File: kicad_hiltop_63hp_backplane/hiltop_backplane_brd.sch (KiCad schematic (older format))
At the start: 20 parts

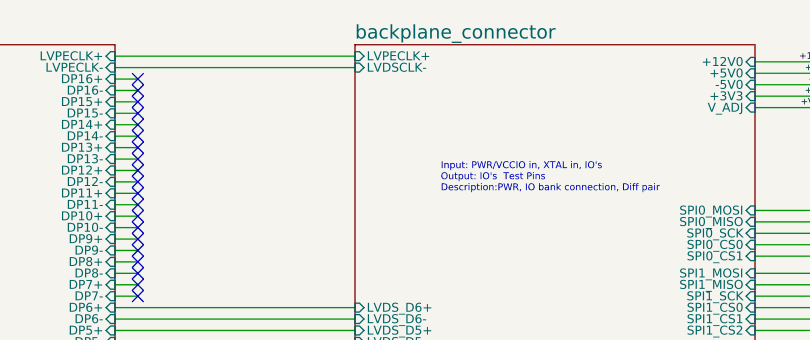
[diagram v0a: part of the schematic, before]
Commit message: pci connector connection moved to bottom layer, FTDI routing and FPGA power routing
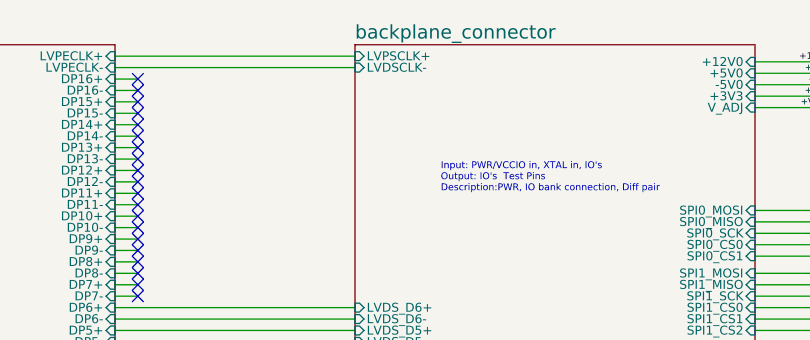
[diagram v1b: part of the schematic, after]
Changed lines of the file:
@@
 F13 "LVDS_D1+" I L 8150 2250 39
 F14 "GND" I R 9900 6250 39
-F15 "LVPECLK+" I L 8150 650 39
+F15 "LVPSCLK+" I L 8150 650 39
 F16 "LVDSCLK-" I L 8150 700 39
 F17 "FPGA_GPIO1" I L 8150 2475 39

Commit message: routing on differential, USB, Power and internconnects
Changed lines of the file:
@@
 F14 "GND" I R 9900 6250 39
 F15 "LVPSCLK+" I L 8150 650 39
-F16 "LVDSCLK-" I L 8150 700 39
+F16 "LVPSCLK-" I L 8150 700 39
 F17 "FPGA_GPIO1" I L 8150 2475 39
 F18 "FPGA_GPIO2" I L 8150 2525 39

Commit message: routing os SODIM and GPIO
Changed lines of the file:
@@
 F35 "MBRD_RESERVED_0" I L 1700 4950 39
 F36 "MBRD_RESERVED_1" I L 1700 5000 39
-F37 "MBRD_RESERVED_2" I R 3700 4950 39
-F38 "MBRD_RESERVED_3" I R 3700 5050 39
+F37 "MBRD_RESERVED_2+" I R 3700 4950 39
+F38 "MBRD_RESERVED_2-" I R 3700 5050 39
 F39 "MBRD_PSEL_0" I L 1700 3525 39
 F40 "MBRD_PSEL_1" I L 1700 3575 39

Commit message: Rev A
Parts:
- R82, R83: symbol device:R -> hiltop_backplane_brd-rescue:R-device
- TP1, TP10, TP11, TP12, TP13, TP16, TP17, TP18, TP19, TP2, TP20, TP3, TP4, TP5, TP6, TP7, TP8, TP9: symbol Connector:TestPoint -> hiltop_backplane_brd-rescue:TestPoint-Connector
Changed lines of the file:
@@
 	7100 4525 8150 4525
 $Comp
-L Connector:TestPoint TP6
+L hiltop_backplane_brd-rescue:TestPoint-Connector TP6
 U 1 1 5C46A039
 P 9975 5050
@@
 $EndComp
 $Comp
-L Connector:TestPoint TP10
+L hiltop_backplane_brd-rescue:TestPoint-Connector TP10
 U 1 1 5C46A4C6
 P 10050 5100
@@
 $EndComp
 $Comp
-L Connector:TestPoint TP7
+L hiltop_backplane_brd-rescue:TestPoint-Connector TP7
 U 1 1 5C46A4E0
 P 9975 5150
@@
 $EndComp
 $Comp
-L Connector:TestPoint TP11
+L hiltop_backplane_brd-rescue:TestPoint-Connector TP11
 U 1 1 5C46A4FC
 P 10050 5200
@@
 $EndComp
 $Comp
-L Connector:TestPoint TP8
+L hiltop_backplane_brd-rescue:TestPoint-Connector TP8
 U 1 1 5C46A522
 P 9975 5250
@@
 $EndComp
 $Comp
-L Connector:TestPoint TP12
+L hiltop_backplane_brd-rescue:TestPoint-Connector TP12
 U 1 1 5C46A542
 P 10050 5300
@@
 $EndComp
 $Comp
-L Connector:TestPoint TP9
+L hiltop_backplane_brd-rescue:TestPoint-Connector TP9
 U 1 1 5C46A566
 P 9975 5350
@@
 $EndComp
 $Comp
-L Connector:TestPoint TP13
+L hiltop_backplane_brd-rescue:TestPoint-Connector TP13
 U 1 1 5C46A590
 P 10050 5400
@@
 	1225 3625 1700 3625
 $Comp
-L Connector:TestPoint TP2
+L hiltop_backplane_brd-rescue:TestPoint-Connector TP2
 U 1 1 5C441846
 P 1275 3675
@@
 $EndComp
 $Comp
-L Connector:TestPoint TP1
+L hiltop_backplane_brd-rescue:TestPoint-Connector TP1
 U 1 1 5C441970
 P 1200 3725
@@
 $EndComp
 $Comp
-L Connector:TestPoint TP3
+L hiltop_backplane_brd-rescue:TestPoint-Connector TP3
 U 1 1 5C4419AA
 P 1275 3775
@@
 	1225 4950 1500 4950
 $Comp
-L Connector:TestPoint TP4
+L hiltop_backplane_brd-rescue:TestPoint-Connector TP4
 U 1 1 5D454C70
 P 1325 4875
@@
 $EndComp
 $Comp
-L Connector:TestPoint TP5
+L hiltop_backplane_brd-rescue:TestPoint-Connector TP5
 U 1 1 5D454D59
 P 1325 5075
@@
 FPGA_RST
 $Comp
-L device:R R82
+L hiltop_backplane_brd-rescue:R-device R82
 U 1 1 5C4B32E3
 P 4200 4950
@@
 $EndComp
 $Comp
-L device:R R83
+L hiltop_backplane_brd-rescue:R-device R83
 U 1 1 5C4B338E
 P 4200 5050
@@
 	4350 4950 4600 4950
 $Comp
-L Connector:TestPoint TP16
+L hiltop_backplane_brd-rescue:TestPoint-Connector TP16
 U 1 1 5C507009
 P 4200 2250
@@
 $EndComp
 $Comp
-L Connector:TestPoint TP19
+L hiltop_backplane_brd-rescue:TestPoint-Connector TP19
 U 1 1 5C507080
 P 4275 2300
@@
 $EndComp
 $Comp
-L Connector:TestPoint TP17
+L hiltop_backplane_brd-rescue:TestPoint-Connector TP17
 U 1 1 5C507107
 P 4200 2350
@@
 $EndComp
 $Comp
-L Connector:TestPoint TP20
+L hiltop_backplane_brd-rescue:TestPoint-Connector TP20
 U 1 1 5C507184
 P 4275 2400
@@
 $EndComp
 $Comp
-L Connector:TestPoint TP18
+L hiltop_backplane_brd-rescue:TestPoint-Connector TP18
 U 1 1 5C507279
 P 4200 2450

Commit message: add latest changes
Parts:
- R82, R83: symbol hiltop_backplane_brd-rescue:R-device -> hiltop_backplane_brd-rescue:R-device-hiltop_backplane_brd-rescue
- TP1, TP10, TP11, TP12, TP13, TP16, TP17, TP18, TP19, TP2, TP20, TP3, TP4, TP5, TP6, TP7, TP8, TP9: symbol hiltop_backplane_brd-rescue:TestPoint-Connector -> hiltop_backplane_brd-rescue:TestPoint-Connector-hiltop_backplane_brd-rescue
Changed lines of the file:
@@
 EESchema Schematic File Version 4
 LIBS:hiltop_backplane_brd-cache
-EELAYER 26 0
+EELAYER 29 0
 EELAYER END
 $Descr A4 11693 8268
 encoding utf-8
 Sheet 1 6
-Title "Project X"
-Date ""
-Rev "Draft"
+Title "63HP HILTOP Backplane"
+Date "2020-02-29"
+Rev "B"
 Comp "Devtank Ltd"
 Comment1 ""
@@
 F99 "USB1_N" I R 9900 4475 39
 F100 "USB1_P" I R 9900 4425 39
-F101 "USB2_N" I R 9900 4525 39
-F102 "USB2_P" I R 9900 4575 39
+F101 "USB2_N" I R 9900 4575 39
+F102 "USB2_P" I R 9900 4525 39
 F103 "USB3_N" I R 9900 4675 39
 F104 "USB3_P" I R 9900 4625 39
@@
 	7100 4525 8150 4525
 $Comp
-L hiltop_backplane_brd-rescue:TestPoint-Connector TP6
+L hiltop_backplane_brd-rescue:TestPoint-Connector-hiltop_backplane_brd-rescue TP6
 U 1 1 5C46A039
 P 9975 5050
@@
 $EndComp
 $Comp
-L hiltop_backplane_brd-rescue:TestPoint-Connector TP10
+L hiltop_backplane_brd-rescue:TestPoint-Connector-hiltop_backplane_brd-rescue TP10
 U 1 1 5C46A4C6
 P 10050 5100
@@
 $EndComp
 $Comp
-L hiltop_backplane_brd-rescue:TestPoint-Connector TP7
+L hiltop_backplane_brd-rescue:TestPoint-Connector-hiltop_backplane_brd-rescue TP7
 U 1 1 5C46A4E0
 P 9975 5150
@@
 $EndComp
 $Comp
-L hiltop_backplane_brd-rescue:TestPoint-Connector TP11
+L hiltop_backplane_brd-rescue:TestPoint-Connector-hiltop_backplane_brd-rescue TP11
 U 1 1 5C46A4FC
 P 10050 5200
@@
 $EndComp
 $Comp
-L hiltop_backplane_brd-rescue:TestPoint-Connector TP8
+L hiltop_backplane_brd-rescue:TestPoint-Connector-hiltop_backplane_brd-rescue TP8
 U 1 1 5C46A522
 P 9975 5250
@@
 $EndComp
 $Comp
-L hiltop_backplane_brd-rescue:TestPoint-Connector TP12
+L hiltop_backplane_brd-rescue:TestPoint-Connector-hiltop_backplane_brd-rescue TP12
 U 1 1 5C46A542
 P 10050 5300
@@
 $EndComp
 $Comp
-L hiltop_backplane_brd-rescue:TestPoint-Connector TP9
+L hiltop_backplane_brd-rescue:TestPoint-Connector-hiltop_backplane_brd-rescue TP9
 U 1 1 5C46A566
 P 9975 5350
@@
 $EndComp
 $Comp
-L hiltop_backplane_brd-rescue:TestPoint-Connector TP13
+L hiltop_backplane_brd-rescue:TestPoint-Connector-hiltop_backplane_brd-rescue TP13
 U 1 1 5C46A590
 P 10050 5400
@@
 	1225 3625 1700 3625
 $Comp
-L hiltop_backplane_brd-rescue:TestPoint-Connector TP2
+L hiltop_backplane_brd-rescue:TestPoint-Connector-hiltop_backplane_brd-rescue TP2
 U 1 1 5C441846
 P 1275 3675
@@
 $EndComp
 $Comp
-L hiltop_backplane_brd-rescue:TestPoint-Connector TP1
+L hiltop_backplane_brd-rescue:TestPoint-Connector-hiltop_backplane_brd-rescue TP1
 U 1 1 5C441970
 P 1200 3725
@@
 $EndComp
 $Comp
-L hiltop_backplane_brd-rescue:TestPoint-Connector TP3
+L hiltop_backplane_brd-rescue:TestPoint-Connector-hiltop_backplane_brd-rescue TP3
 U 1 1 5C4419AA
 P 1275 3775
@@
 	1225 4950 1500 4950
 $Comp
-L hiltop_backplane_brd-rescue:TestPoint-Connector TP4
+L hiltop_backplane_brd-rescue:TestPoint-Connector-hiltop_backplane_brd-rescue TP4
 U 1 1 5D454C70
 P 1325 4875
@@
 $EndComp
 $Comp
-L hiltop_backplane_brd-rescue:TestPoint-Connector TP5
+L hiltop_backplane_brd-rescue:TestPoint-Connector-hiltop_backplane_brd-rescue TP5
 U 1 1 5D454D59
 P 1325 5075
@@
 FPGA_RST
 $Comp
-L hiltop_backplane_brd-rescue:R-device R82
+L hiltop_backplane_brd-rescue:R-device-hiltop_backplane_brd-rescue R82
 U 1 1 5C4B32E3
 P 4200 4950
@@
 $EndComp
 $Comp
-L hiltop_backplane_brd-rescue:R-device R83
+L hiltop_backplane_brd-rescue:R-device-hiltop_backplane_brd-rescue R83
 U 1 1 5C4B338E
 P 4200 5050
@@
 	4350 4950 4600 4950
 $Comp
-L hiltop_backplane_brd-rescue:TestPoint-Connector TP16
+L hiltop_backplane_brd-rescue:TestPoint-Connector-hiltop_backplane_brd-rescue TP16
 U 1 1 5C507009
 P 4200 2250
@@
 $EndComp
 $Comp
-L hiltop_backplane_brd-rescue:TestPoint-Connector TP19
+L hiltop_backplane_brd-rescue:TestPoint-Connector-hiltop_backplane_brd-rescue TP19
 U 1 1 5C507080
 P 4275 2300
@@
 $EndComp
 $Comp
-L hiltop_backplane_brd-rescue:TestPoint-Connector TP17
+L hiltop_backplane_brd-rescue:TestPoint-Connector-hiltop_backplane_brd-rescue TP17
 U 1 1 5C507107
 P 4200 2350
@@
 $EndComp
 $Comp
-L hiltop_backplane_brd-rescue:TestPoint-Connector TP20
+L hiltop_backplane_brd-rescue:TestPoint-Connector-hiltop_backplane_brd-rescue TP20
 U 1 1 5C507184
 P 4275 2400
@@
 $EndComp
 $Comp
-L hiltop_backplane_brd-rescue:TestPoint-Connector TP18
+L hiltop_backplane_brd-rescue:TestPoint-Connector-hiltop_backplane_brd-rescue TP18
 U 1 1 5C507279
 P 4200 2450
@@
 F116 "UART_CTS" I L 4600 5850 39
 F117 "UART_RTS" I L 4600 5900 39
-F118 "GPIO_56" I L 4600 3825 39
-F119 "GPIO_55" I L 4600 3875 39
+F118 "GPIO_56" I L 4600 3875 39
+F119 "GPIO_55" I L 4600 3825 39
 $EndSheet
 Wire Wire Line

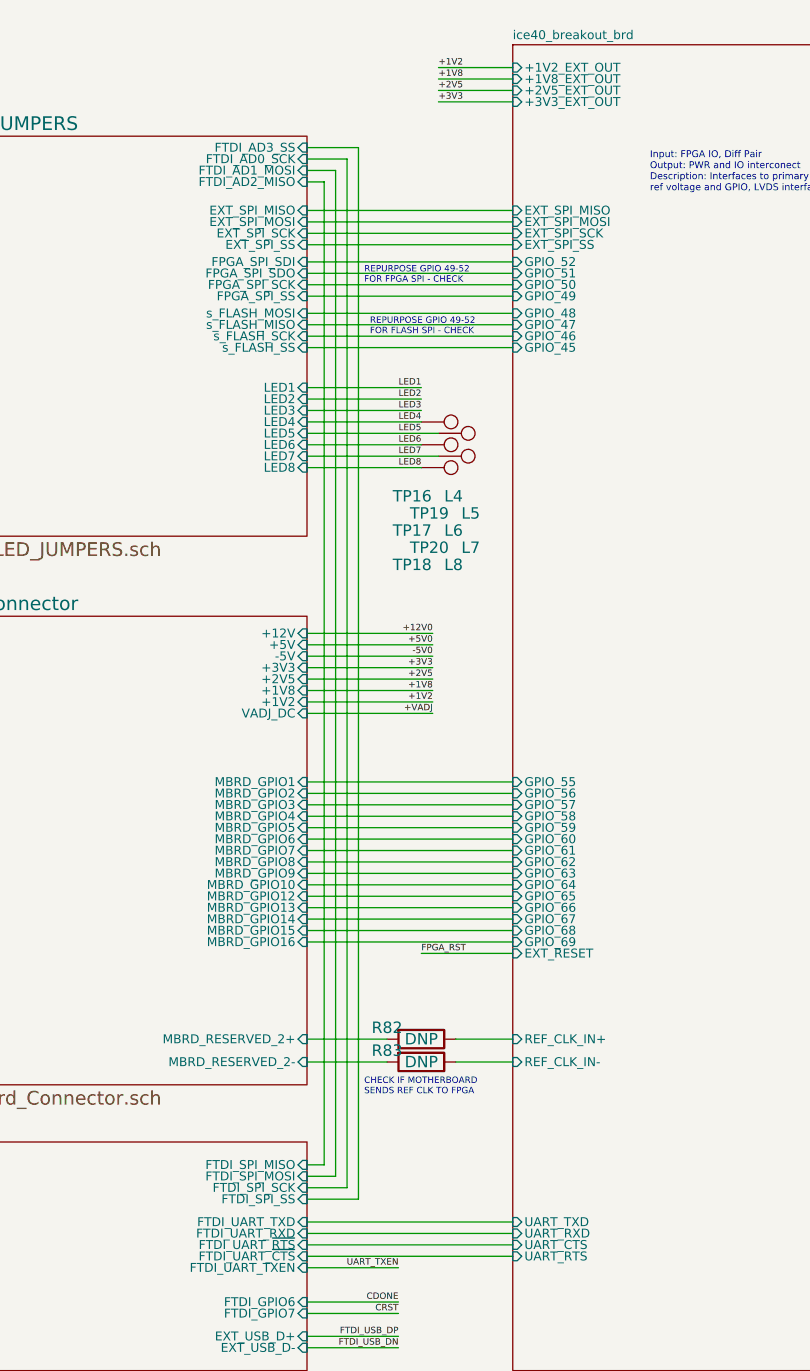
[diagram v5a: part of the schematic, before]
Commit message: started simplifications to design
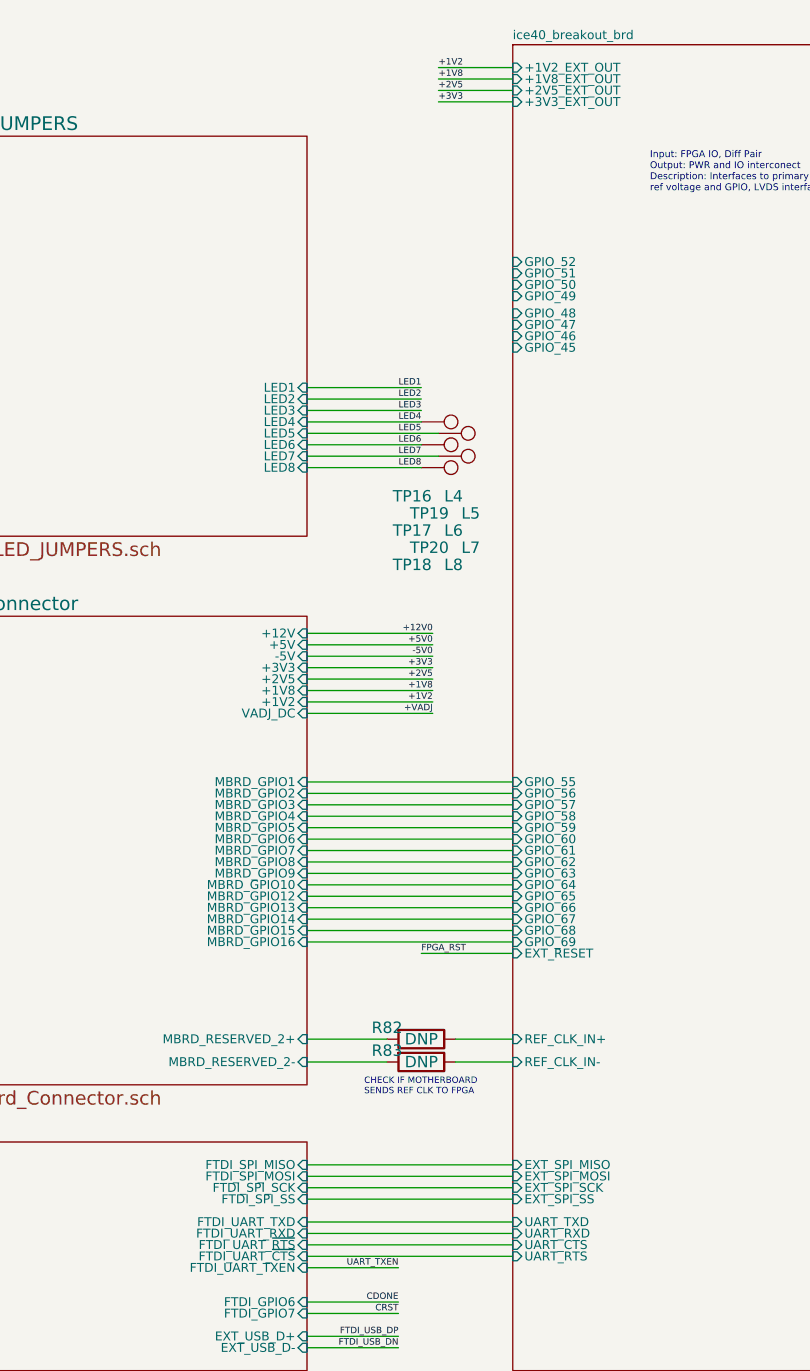
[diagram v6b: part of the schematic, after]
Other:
- note removed: "REPURPOSE GPIO 49-52 \nFOR FLASH SPI - CHECK"
- note removed: "REPURPOSE GPIO 49-52 \nFOR FPGA SPI - CHECK"
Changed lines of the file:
@@
 EESchema Schematic File Version 4
-LIBS:hiltop_backplane_brd-cache
-EELAYER 29 0
+EELAYER 30 0
 EELAYER END
 $Descr A4 11693 8268
@@
 CHECK IF MOTHERBOARD \nSENDS REF CLK TO FPGA
 Wire Wire Line
-	3700 5500 3775 5500
-Wire Wire Line
-	3775 5500 3775 1200
-Wire Wire Line
-	3775 1200 3700 1200
-Wire Wire Line
-	3700 5550 3825 5550
-Wire Wire Line
-	3825 5550 3825 1150
-Wire Wire Line
-	3825 1150 3700 1150
-Wire Wire Line
-	3700 5600 3875 5600
-Wire Wire Line
-	3875 5600 3875 1100
-Wire Wire Line
-	3875 1100 3700 1100
-Wire Wire Line
-	3700 5650 3925 5650
-Wire Wire Line
-	3925 5650 3925 1050
-Wire Wire Line
-	3925 1050 3700 1050
-Wire Wire Line
-	3700 1325 4600 1325
-Wire Wire Line
-	3700 1375 4600 1375
-Wire Wire Line
-	3700 1425 4600 1425
-Wire Wire Line
-	3700 1475 4600 1475
-Wire Wire Line
-	3700 1550 4600 1550
-Wire Wire Line
-	3700 1600 4600 1600
-Wire Wire Line
-	3700 1650 4600 1650
-Wire Wire Line
-	3700 1700 4600 1700
-Text Notes 3950 1650 0    28   ~ 0
-REPURPOSE GPIO 49-52 \nFOR FPGA SPI - CHECK
-Wire Wire Line
-	3700 1775 4600 1775
-Wire Wire Line
-	3700 1825 4600 1825
-Wire Wire Line
-	3700 1875 4600 1875
-Wire Wire Line
-	3700 1925 4600 1925
-Text Notes 3975 1875 0    28   ~ 0
-REPURPOSE GPIO 49-52 \nFOR FLASH SPI - CHECK
-Wire Wire Line
 	3700 2100 4200 2100
 Wire Wire Line
@@
 Wire Wire Line
 	1325 5075 1500 5075
-$Sheet
-S 1700 1000 2000 1750
-U 5A077C30
-F0 "USB_HUB_LED_JUMPERS" 60
-F1 "USB_HUB_LED_JUMPERS.sch" 60
-F2 "+3V3_IN" I L 1700 1075 39
-F3 "FTDI_AD2_MISO" I R 3700 1200 39
-F4 "EXT_SPI_MISO" I R 3700 1325 39
-F5 "FTDI_AD1_MOSI" I R 3700 1150 39
-F6 "EXT_SPI_MOSI" I R 3700 1375 39
-F7 "FTDI_AD0_SCK" I R 3700 1100 39
-F8 "EXT_SPI_SCK" I R 3700 1425 39
-F9 "FTDI_AD3_SS" I R 3700 1050 39
-F10 "EXT_SPI_SS" I R 3700 1475 39
-F11 "FPGA_SPI_SDO" I R 3700 1600 39
-F12 "s_FLASH_MOSI" I R 3700 1775 39
-F13 "s_FLASH_MISO" I R 3700 1825 39
-F14 "s_FLASH_SCK" I R 3700 1875 39
-F15 "FPGA_SPI_SCK" I R 3700 1650 39
-F16 "FPGA_SPI_SS" I R 3700 1700 39
-F17 "FPGA_SPI_SDI" I R 3700 1550 39
-F18 "s_FLASH_SS" I R 3700 1925 39
-F19 "GND" I L 1700 2700 39
-F20 "USB_HUB1_P" I L 1700 1450 39
-F21 "USB_HUB2_P" I L 1700 1625 39
-F22 "USB_HUB3_P" I L 1700 1800 39
-F23 "USB_HUB4_P" I L 1700 1975 39
-F24 "USB_HUB5_P" I L 1700 2150 39
-F25 "USB_HUB6_P" I L 1700 2325 39
-F26 "USB_HUB7_P" I L 1700 2500 39
-F27 "USB_HUB1_N" I L 1700 1500 39
-F28 "USB_HUB2_N" I L 1700 1675 39
-F29 "USB_HUB3_N" I L 1700 1850 39
-F30 "USB_HUB4_N" I L 1700 2025 39
-F31 "USB_HUB5_N" I L 1700 2200 39
-F32 "USB_HUB6_N" I L 1700 2375 39
-F33 "USB_HUB7_N" I L 1700 2550 39
-F34 "USB_~OSC6" I L 1700 2450 39
-F35 "USB_~OSC5" I L 1700 2275 39
-F36 "USB_~OSC4" I L 1700 2100 39
-F37 "USB_~OSC3" I L 1700 1925 39
-F38 "USB_~OSC2" I L 1700 1750 39
-F39 "USB_~OSC1" I L 1700 1575 39
-F40 "LED1" I R 3700 2100 39
-F41 "LED2" I R 3700 2150 39
-F42 "LED3" I R 3700 2200 39
-F43 "LED4" I R 3700 2250 39
-F44 "LED5" I R 3700 2300 39
-F45 "LED6" I R 3700 2350 39
-F46 "LED7" I R 3700 2400 39
-F47 "LED8" I R 3700 2450 39
-F48 "USB_~RESET" I L 1700 1375 39
-F49 "USB_~OSC7" I L 1700 2625 39
-F50 "USB_D+" I L 1700 1175 39
-F51 "USB_D-" I L 1700 1250 39
-$EndSheet
 Text Label 4275 700  0    28   ~ 0
 +1V2
@@
 F38 "DP15+" I R 7100 850 39
 F39 "DP16+" I R 7100 750 39
-F40 "EXT_SPI_MISO" I L 4600 1325 39
-F41 "EXT_SPI_MOSI" I L 4600 1375 39
-F42 "EXT_SPI_SCK" I L 4600 1425 39
-F43 "EXT_SPI_SS" I L 4600 1475 39
+F40 "EXT_SPI_MISO" I L 4600 5500 39
+F41 "EXT_SPI_MOSI" I L 4600 5550 39
+F42 "EXT_SPI_SCK" I L 4600 5600 39
+F43 "EXT_SPI_SS" I L 4600 5650 39
 F44 "EXT_RESET" I L 4600 4575 39
 F45 "REF_CLK_IN+" I L 4600 4950 39
@@
 Wire Wire Line
 	3700 2400 4275 2400
+$Sheet
+S 1700 1000 2000 1750
+U 5A077C30
+F0 "USB_HUB_LED_JUMPERS" 60
+F1 "USB_HUB_LED_JUMPERS.sch" 60
+F2 "+3V3_IN" I L 1700 1075 39
+F15 "GND" I L 1700 2700 39
+F16 "USB_HUB1_P" I L 1700 1450 39
+F17 "USB_HUB2_P" I L 1700 1625 39
+F18 "USB_HUB3_P" I L 1700 1800 39
+F19 "USB_HUB4_P" I L 1700 1975 39
+F20 "USB_HUB5_P" I L 1700 2150 39
+F21 "USB_HUB6_P" I L 1700 2325 39
+F22 "USB_HUB7_P" I L 1700 2500 39
+F23 "USB_HUB1_N" I L 1700 1500 39
+F24 "USB_HUB2_N" I L 1700 1675 39
+F25 "USB_HUB3_N" I L 1700 1850 39
+F26 "USB_HUB4_N" I L 1700 2025 39
+F27 "USB_HUB5_N" I L 1700 2200 39
+F28 "USB_HUB6_N" I L 1700 2375 39
+F29 "USB_HUB7_N" I L 1700 2550 39
+F30 "USB_~OSC6" I L 1700 2450 39
+F31 "USB_~OSC5" I L 1700 2275 39
+F32 "USB_~OSC4" I L 1700 2100 39
+F33 "USB_~OSC3" I L 1700 1925 39
+F34 "USB_~OSC2" I L 1700 1750 39
+F35 "USB_~OSC1" I L 1700 1575 39
+F36 "LED1" I R 3700 2100 39
+F37 "LED2" I R 3700 2150 39
+F38 "LED3" I R 3700 2200 39
+F39 "LED4" I R 3700 2250 39
+F40 "LED5" I R 3700 2300 39
+F41 "LED6" I R 3700 2350 39
+F42 "LED7" I R 3700 2400 39
+F43 "LED8" I R 3700 2450 39
+F44 "USB_~RESET" I L 1700 1375 39
+F45 "USB_~OSC7" I L 1700 2625 39
+F46 "USB_D+" I L 1700 1175 39
+F47 "USB_D-" I L 1700 1250 39
+$EndSheet
+Wire Wire Line
+	3700 5500 4600 5500
+Wire Wire Line
+	3700 5550 4600 5550
+Wire Wire Line
+	3700 5600 4600 5600
+Wire Wire Line
+	3700 5650 4600 5650
 $EndSCHEMATC
